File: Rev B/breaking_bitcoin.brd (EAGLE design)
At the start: 53.3 x 63.5 mm, 66 parts, among them J1 M20-9992046, J2 M20-9992046, J3 M20-9992046, J4 TC2050-IDC-NLFP, J5 DNP, J6 DNP, J7 ZX80-B-5P, Q1 DMG2302UK, U1 STM32F205RE, U2 MCP1703AT-3302E/CB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

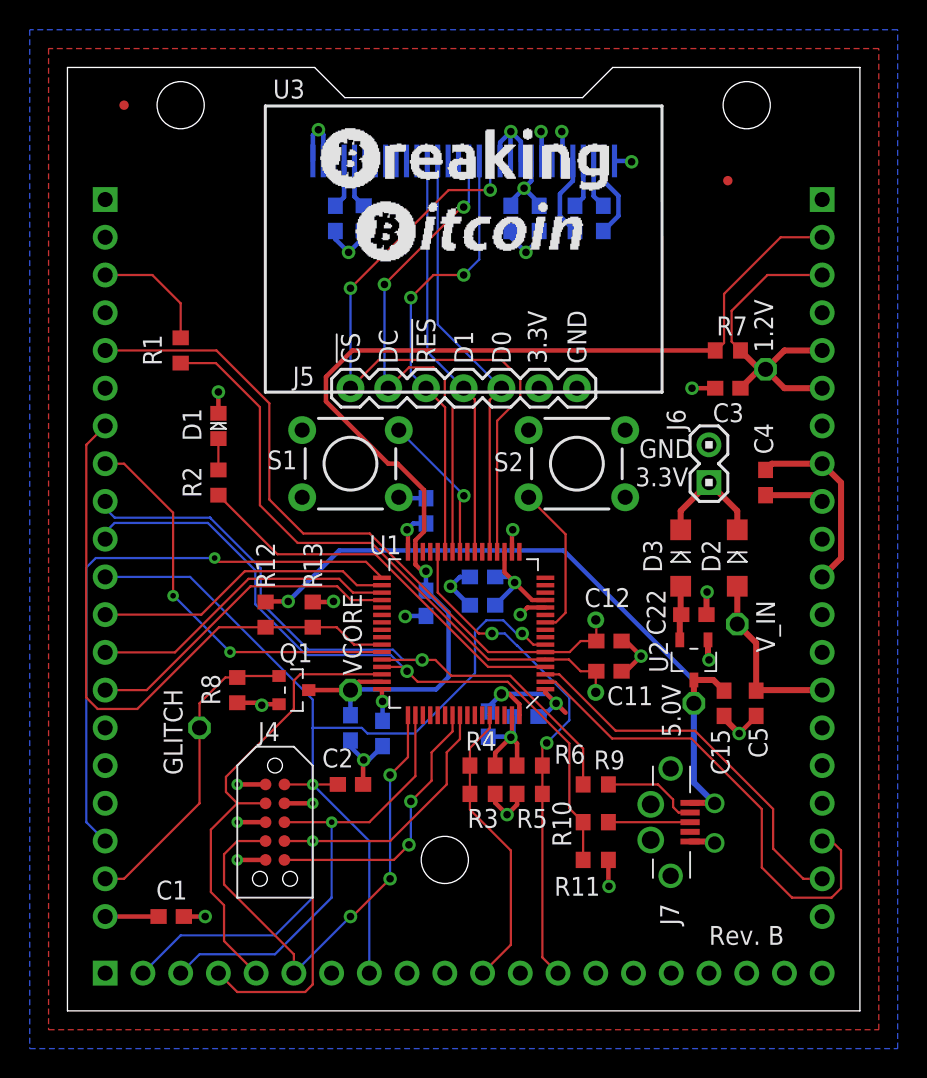
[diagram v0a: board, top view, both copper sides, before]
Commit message: Fixing south bridge for the Rev. B
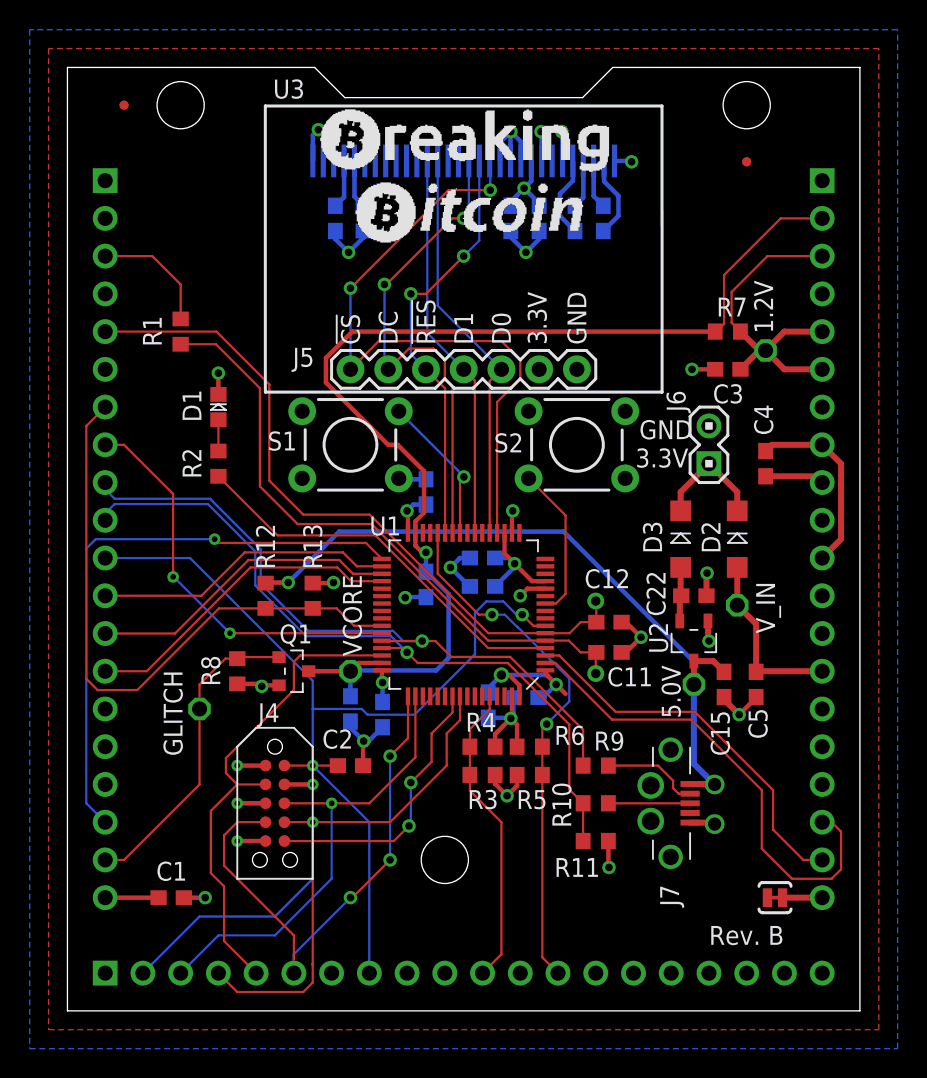
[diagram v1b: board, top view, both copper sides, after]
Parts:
- added JP1: JUMPER-PAD-2-NC_BY_TRACE, SparkFun-Passives:PAD-JUMPER-2-NC_BY_TRACE_YES_SILK
- moved FD2 1.80 mm to (45.7, 57.1)
- moved C16 1.27 mm to (28.3, 20.6)
- moved C3 1.27 mm to (44.5, 43.2)
- moved C6 1.27 mm to (24.1, 28.7)
- moved D1 1.27 mm to (10.2, 40.6)
- moved J5 1.27 mm to (19.1, 43.2)
- moved J6 1.27 mm to (43.2, 38.1)
- moved S1 1.27 mm to (19.1, 38.1)
- moved S2 1.27 mm to (34.3, 38.1)
- moved TP1 1.27 mm to (47.0, 44.5)
- moved U$2 1.27 mm to (5.08, 33.0)
- moved U$3 1.27 mm to (36.8, 40.0)
- moved U1 1.27 mm to (26.7, 26.7)
- moved C2 1.27 mm to (19.1, 16.5)
- moved J4 1.27 mm to (14.0, 14.0)
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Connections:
- new net N$12: J3.20, JP1.1
- net 3.3V: now also JP1.2; no longer J3.20
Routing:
- net N$12: track 0.00 -> 2.67 mm
- net JTAG_TCK: track 33.7 -> 36.3 mm
- net OLED_!RES: track 30.4 -> 28.5 mm
- net OLED_!CS: track 46.0 -> 44.6 mm
- net JTAG_TDO: track 34.2 -> 35.5 mm
- net OLED_D1: track 27.6 -> 26.4 mm
- net OLED_D0: track 28.4 -> 27.1 mm
- net BOOT1: track 34.3 -> 35.5 mm
- net JTAG_TMS: track 31.9 -> 33.2 mm
- net !RESET: track 62.3 -> 63.5 mm
- net OLED_DC: track 34.4 -> 33.6 mm
- net BOOT0: track 19.9 -> 20.6 mm
- net JTAG_TDI: track 31.5 -> 32.1 mm
- net JTAG_TRST: track 34.9 -> 35.4 mm
